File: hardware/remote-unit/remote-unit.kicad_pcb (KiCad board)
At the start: 2 copper layers, 94 x 56.3 mm, 60 parts, among them J1 SOL_A, J2 RF Module, J3 ICSP, J5 SOL_B, J6 PWR 12V, J7 UART, J8 RS485, J9 SOLAR, Q1 N >1A@4VGS, Q2 PNP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

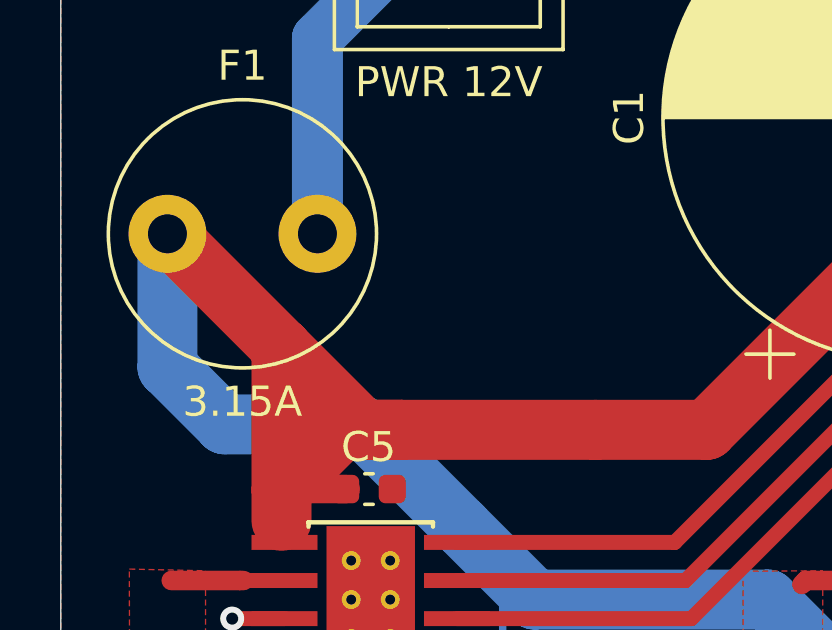
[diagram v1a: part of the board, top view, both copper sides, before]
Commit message: Add SMT fuse to remote unit
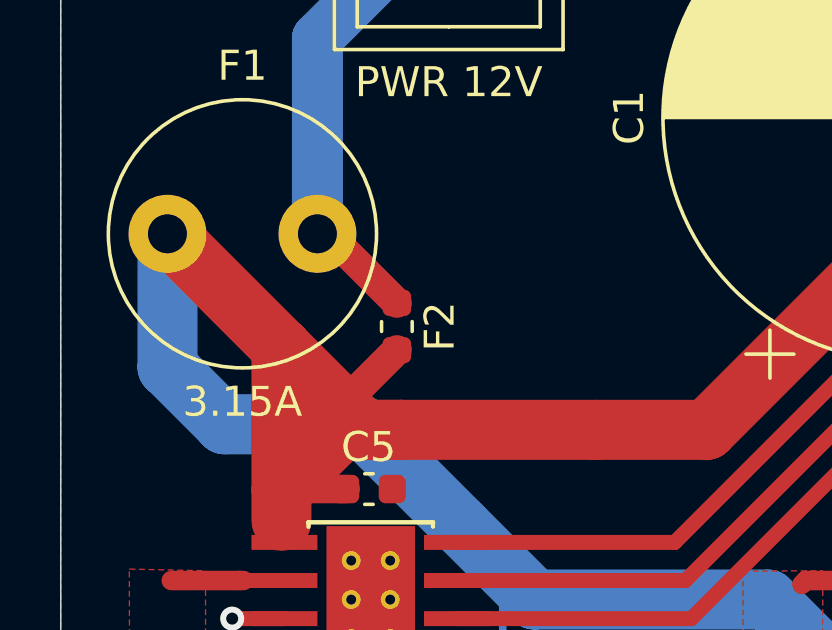
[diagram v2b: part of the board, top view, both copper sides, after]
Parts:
- added F2: Fuse_Small, Fuse:Fuse_0603_1608Metric, F.Cu at (93.5, 90.2)
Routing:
- net Net-(J6-Pin_1): track 10.9 -> 14.5 mm
- net +12V: track 196.8 -> 199.4 mm
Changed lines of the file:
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@@
 			)
 		)
-		(property "FT Rotation Offset" "90"
+		(property "FT Rotation Offset" "-90"
 			(at 0 0 180)
 			(unlocked yes)
@@
 			)
 		)
-		(property "FT Rotation Offset" "90"
+		(property "FT Rotation Offset" "-90"
 			(at 0 0 180)
 			(unlocked yes)
@@
 			)
 		)
-		(property "FT Rotation Offset" "90"
+		(property "FT Rotation Offset" "-90"
 			(at 0 0 0)
 			(unlocked yes)
@@
 		(sheetname "/")
 		(sheetfile "remote-unit.kicad_sch")
-		(attr through_hole)
+		(attr through_hole exclude_from_bom)
 		(fp_line
 			(start -2.85 -2.75)
@@
 		)
 	)
+	(footprint "Fuse:Fuse_0603_1608Metric"
+		(layer "F.Cu")
+		(at 93.5 90.2125 -90)
+		(descr "Fuse SMD 0603 (1608 Metric), square (rectangular) end terminal, IPC-7351 nominal, (Body size source: http://www.tortai-tech.com/upload/download/2011102023233369053.pdf), generated with kicad-footprint-generator")
+		(tags "fuse")
+		(property "Reference" "F2"
+			(at 0 -1.43 90)
+			(layer "F.SilkS")
+			(effects
+				(font
+					(size 1 1)
+					(thickness 0.15)
+				)
+			)
+		)
+		(property "Value" "Fuse_Small"
+			(at 0 1.43 90)
+			(layer "F.Fab")
+			(effects
+				(font
+					(size 1 1)
+					(thickness 0.15)
+				)
+			)
+		)
+		(property "Datasheet" "https://www.lcsc.com/datasheet/C163117.pdf"
+			(at 0 0 90)
+			(layer "F.Fab")
+			(hide yes)
+			(effects
+				(font
+					(size 1.27 1.27)
+					(thickness 0.15)
+				)
+			)
+		)
+		(property "Description" "Fuse, small symbol"
+			(at 0 0 90)
+			(layer "F.Fab")
+			(hide yes)
+			(effects
+				(font
+					(size 1.27 1.27)
+					(thickness 0.15)
+				)
+			)
+		)
+		(property "JLCPCB Part" "C163117"
+			(at 0 0 270)
+			(unlocked yes)
+			(layer "F.Fab")
+			(hide yes)
+			(effects
+				(font
+					(size 1 1)
+					(thickness 0.15)
+				)
+			)
+		)
+		(property ki_fp_filters "*Fuse*")
+		(sheetname "/")
+		(sheetfile "remote-unit.kicad_sch")
+		(attr smd)
+		(fp_line
+			(start -0.162779 0.51)
+			(end 0.162779 0.51)
+			(stroke
+				(width 0.12)
+				(type solid)
+			)
+			(layer "F.SilkS")
+		)
+		(fp_line
+			(start -0.162779 -0.51)
+			(end 0.162779 -0.51)
+			(stroke
+				(width 0.12)
+				(type solid)
+			)
+			(layer "F.SilkS")
+		)
+		(fp_line
+			(start -1.48 0.73)
+			(end -1.48 -0.73)
+			(stroke
+				(width 0.05)
+				(type solid)
+			)
+			(layer "F.CrtYd")
+		)
+		(fp_line
+			(start 1.48 0.73)
+			(end -1.48 0.73)
+			(stroke
+				(width 0.05)
+				(type solid)
+			)
+			(layer "F.CrtYd")
+		)
+		(fp_line
+			(start -1.48 -0.73)
+			(end 1.48 -0.73)
+			(stroke
+				(width 0.05)
+				(type solid)
+			)
+			(layer "F.CrtYd")
+		)
+		(fp_line
+			(start 1.48 -0.73)
+			(end 1.48 0.73)
+			(stroke
+				(width 0.05)
+				(type solid)
+			)
+			(layer "F.CrtYd")
+		)
+		(fp_line
+			(start -0.8 0.4)
+			(end -0.8 -0.4)
+			(stroke
+				(width 0.1)
+				(type solid)
+			)
+			(layer "F.Fab")
+		)
+		(fp_line
+			(start 0.8 0.4)
+			(end -0.8 0.4)
+			(stroke
+				(width 0.1)
+				(type solid)
+			)
+			(layer "F.Fab")
+		)
+		(fp_line
+			(start -0.8 -0.4)
+			(end 0.8 -0.4)
+			(stroke
+				(width 0.1)
+				(type solid)
+			)
+			(layer "F.Fab")
+		)
+		(fp_line
+			(start 0.8 -0.4)
+			(end 0.8 0.4)
+			(stroke
+				(width 0.1)
+				(type solid)
+			)
+			(layer "F.Fab")
+		)
+		(fp_text user "${REFERENCE}"
+			(at 0 0 90)
+			(layer "F.Fab")
+			(effects
+				(font
+					(size 0.4 0.4)
+					(thickness 0.06)
+				)
+			)
+		)
+		(pad "1" smd roundrect
+			(at -0.7875 0 270)
+			(size 0.875 0.95)
+			(layers "F.Cu" "F.Mask" "F.Paste")
+			(roundrect_rratio 0.25)
+			(net 30 "Net-(J6-Pin_1)")
+			(pintype "passive")
+		)
+		(pad "2" smd roundrect
+			(at 0.7875 0 270)
+			(size 0.875 0.95)
+			(layers "F.Cu" "F.Mask" "F.Paste")
+			(roundrect_rratio 0.25)
+			(net 2 "+12V")
+			(pintype "passive")
+		)
+		(embedded_fonts no)
+		(model "${KICAD9_3DMODEL_DIR}/Fuse.3dshapes/Fuse_0603_1608Metric.step"
+			(offset
+				(xyz 0 0 0)
+			)
+			(scale
+				(xyz 1 1 1)
+			)
+			(rotate
+				(xyz 0 0 0)
+			)
+		)
+	)
 	(footprint "Package_TO_SOT_SMD:SOT-23"
 		(layer "F.Cu")
@@
 	)
 	(segment
+		(start 91.615 92.885)
+		(end 93.5 91)
+		(width 1)
+		(layer "F.Cu")
+		(net 2)
+	)
+	(segment
 		(start 100.116988 93.65599)
 		(end 93.65599 93.65599)
@@
 	)
 	(segment
+		(start 90.852 87.122)
+		(end 91.197 87.122)
+		(width 1.7)
+		(layer "F.Cu")
+		(net 30)
+	)
+	(segment
+		(start 91.197 87.122)
+		(end 93.5 89.425)
+		(width 1)
+		(layer "F.Cu")
+		(net 30)
+	)
+	(segment

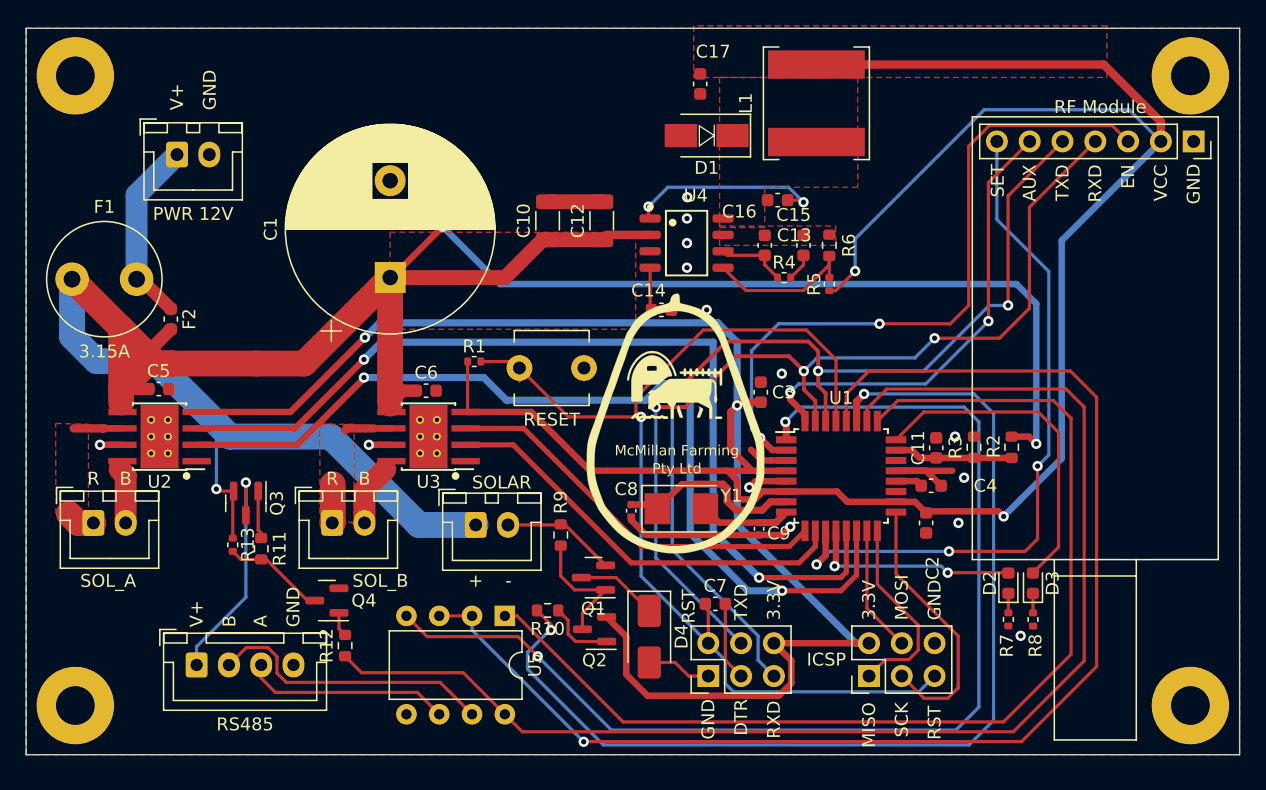
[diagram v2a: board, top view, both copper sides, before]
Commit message: Use SMT MAX3485 for remote unit
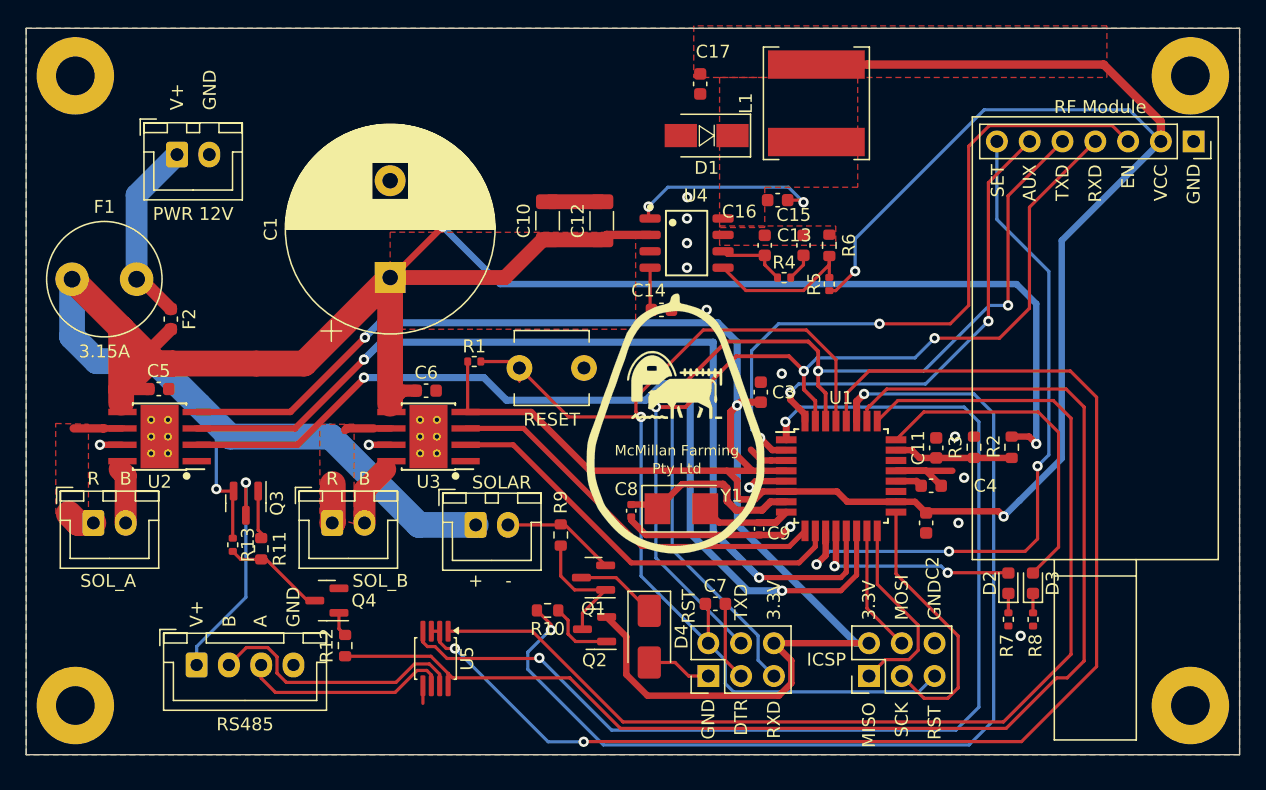
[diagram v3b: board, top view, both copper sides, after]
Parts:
- U5: footprint Package_DIP:DIP-8_W7.62mm -> Package_SO:MSOP-8_3x3mm_P0.65mm
- moved U5 6.30 mm to (114.0, 116.5)
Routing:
- net /PC2: track 83.9 -> 87.8 mm
- net Net-(J8-Pin_2): track 22.3 -> 20.6 mm
- net GND: track 40.4 -> 41.7 mm
- net /PD3: track 88.2 -> 86.9 mm
- net /PC3: track 100.7 -> 101.4 mm
- net /PC5: vias 1 -> 2

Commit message: Add remote unit current sense resistors
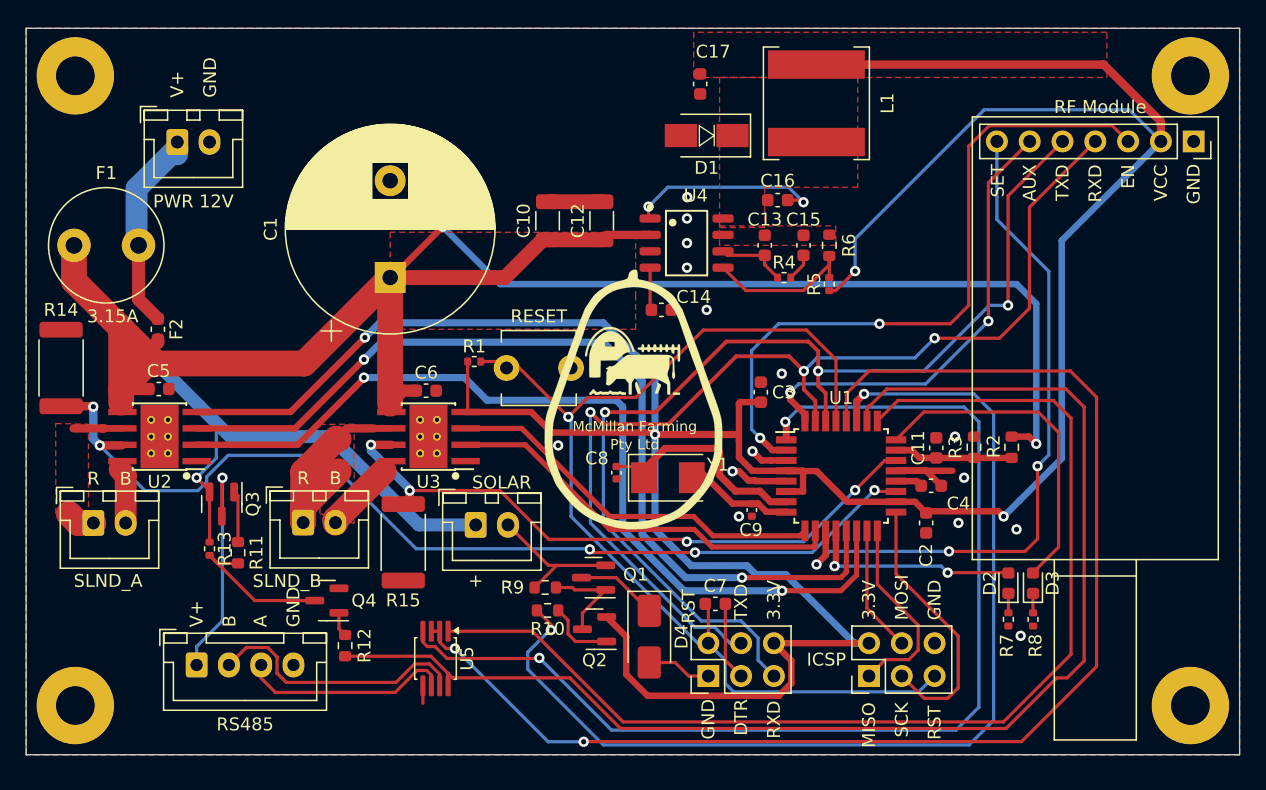
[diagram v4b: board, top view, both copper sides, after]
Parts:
- added R14: 100m, Resistor_SMD:R_2512_6332Metric, F.Cu at (85.0, 94.0)
- added R15: 100m, Resistor_SMD:R_2512_6332Metric, F.Cu at (111.5, 107.5)
- J1: value SOL_A -> SLND_A
- J5: value SOL_B -> SLND_B
- moved R9 4.24 mm to (122.5, 111.0), turned to 180 degrees
- moved G*** 3.75 mm to (129.5, 96.5)
- moved C8 3.16 mm to (128.0, 102.1)
- moved F1 2.63 mm to (86.0, 84.5)
- moved Y1 2.62 mm to (132.0, 102.5)
- moved J5 2.25 mm to (103.8, 106.0)
- moved Q3 1.87 mm to (97.5, 104.5)
- moved R11 1.82 mm to (98.7, 108.3)
- moved R13 1.82 mm to (96.5, 108.0)
- moved C9 1.56 mm to (138.5, 105.0)
- moved F2 1.27 mm to (92.5, 91.0)
- moved SW1 1.00 mm to (122.0, 94.0)
- moved J6 0.97 mm to (94.0, 76.5)
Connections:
- U1 pad 19: unconnected-(U1-ADC6-Pad19) -> /ADC6
- U1 pad 22: unconnected-(U1-ADC7-Pad22) -> /ADC7
- U2 pad 7: GND -> /ADC6
- U3 pad 7: GND -> /ADC7
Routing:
- net /ADC6: track 0.00 -> 77.1 mm, vias 0 -> 5
- net /ADC7: track 0.00 -> 49.5 mm, vias 0 -> 4
- net GND: track 41.7 -> 26.3 mm, vias 14 -> 15
- net /SOL_B1: track 6.66 -> 16.3 mm
- net /TXD: track 73.4 -> 82.5 mm
- net /RXD: track 75.2 -> 83.8 mm
- net +3.3V: track 264.4 -> 258.9 mm
- net Net-(Q4-C): track 7.93 -> 12.1 mm
- net Net-(U1-XTAL2/PB7): track 7.05 -> 9.54 mm
- net /SOLAR_LOW: track 8.90 -> 11.3 mm
- net Net-(Q1-G): track 10.1 -> 7.72 mm
- net Net-(U1-XTAL1/PB6): track 14.6 -> 16.8 mm
- net /DRV_A2: track 71.8 -> 69.6 mm
- net /DRV_A1: track 72.6 -> 71.0 mm
- net Net-(J6-Pin_1): track 14.5 -> 15.7 mm
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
